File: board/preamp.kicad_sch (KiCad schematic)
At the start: 16 parts, among them SW2 200MDP1T2B2M2, U5 MAX4062

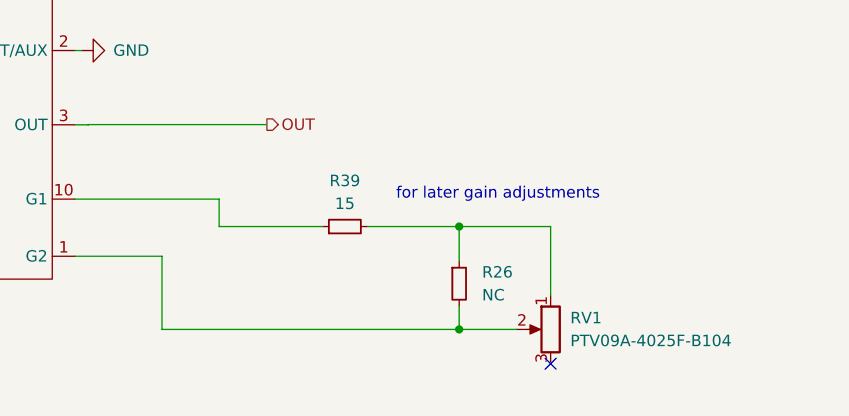
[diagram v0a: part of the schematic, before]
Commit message: option for poti inversion and some missing connections
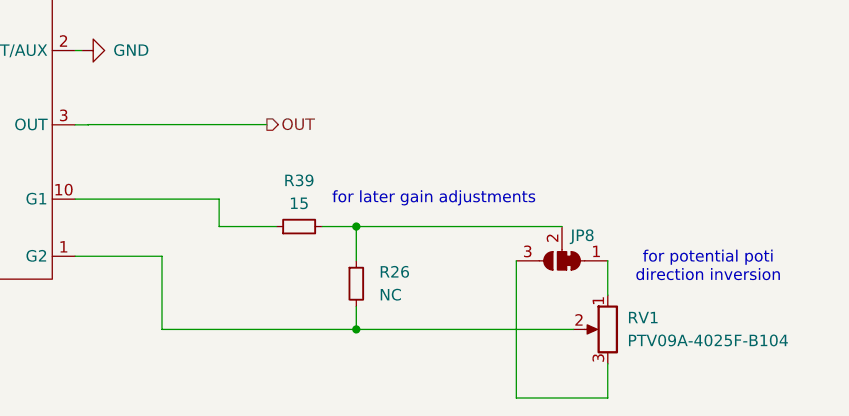
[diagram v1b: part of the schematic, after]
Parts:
- added JP8: SolderJumper_3_Bridged12, Jumper:SolderJumper-3_P1.3mm_Bridged12_RoundedPad1.0x1.5mm, symbol Jumper:SolderJumper_3_Bridged12
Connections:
- net at R26.1, R39.2: now also JP8.2 (C); no longer RV1.1
- net at RV1.3: now also JP8.3 (B)
- new net: JP8.1 (A), RV1.1
- no-connect marks 1 -> 0
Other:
- note added: "for potential poti direction inversion"
- moved on the sheet: R26, R39, RV1
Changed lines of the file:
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@@
 	(paper "A4")
+	(junction
+		(at 228.6 99.06)
+		(diameter 0)
+		(color 0 0 0 0)
+	)
 	(junction
 		(at 154.94 62.23)
@@
 	)
 	(junction
-		(at 240.03 87.63)
-		(diameter 0)
-		(color 0 0 0 0)
-	)
-	(junction
 		(at 78.486 79.629)
 		(diameter 0)
@@
 	)
 	(junction
-		(at 240.03 99.06)
-		(diameter 0)
-		(color 0 0 0 0)
-	)
-	(junction
 		(at 180.34 46.99)
 		(diameter 0)
@@
 	)
 	(junction
+		(at 228.6 87.63)
+		(diameter 0)
+		(color 0 0 0 0)
+	)
+	(junction
 		(at 92.583 83.693)
 		(diameter 0)
 		(color 0 0 0 0)
 	)
-	(no_connect
-		(at 250.19 102.87)
-	)
 	(wire
 		(pts
@@
 	(wire
 		(pts
+			(xy 256.54 102.87) (xy 256.54 106.68)
+		)
+		(stroke
+			(width 0)
+			(type default)
+		)
+	)
+	(wire
+		(pts
 			(xy 180.34 44.45) (xy 180.34 46.99)
 		)
@@
 	(wire
 		(pts
-			(xy 250.19 95.25) (xy 250.19 87.63)
+			(xy 256.54 91.44) (xy 256.54 95.25)
 		)
 		(stroke
@@
 	(wire
 		(pts
-			(xy 240.03 99.06) (xy 240.03 96.52)
+			(xy 246.38 106.68) (xy 256.54 106.68)
+		)
+		(stroke
+			(width 0)
+			(type default)
+		)
+	)
+	(wire
+		(pts
+			(xy 228.6 99.06) (xy 228.6 96.52)
 		)
 		(stroke
@@
 	(wire
 		(pts
-			(xy 240.03 87.63) (xy 240.03 91.44)
+			(xy 228.6 87.63) (xy 228.6 91.44)
 		)
 		(stroke
@@
 	(wire
 		(pts
-			(xy 229.87 87.63) (xy 240.03 87.63)
+			(xy 224.79 87.63) (xy 228.6 87.63)
 		)
 		(stroke
@@
 	(wire
 		(pts
+			(xy 246.38 91.44) (xy 246.38 106.68)
+		)
+		(stroke
+			(width 0)
+			(type default)
+		)
+	)
+	(wire
+		(pts
 			(xy 185.42 49.53) (xy 185.42 46.99)
 		)
@@
 	(wire
 		(pts
-			(xy 240.03 87.63) (xy 250.19 87.63)
-		)
-		(stroke
-			(width 0)
-			(type default)
-		)
-	)
-	(wire
-		(pts
 			(xy 144.78 62.23) (xy 148.59 62.23)
 		)
@@
 	(wire
 		(pts
-			(xy 207.01 99.06) (xy 240.03 99.06)
+			(xy 207.01 99.06) (xy 228.6 99.06)
 		)
 		(stroke
@@
 	(wire
 		(pts
+			(xy 228.6 87.63) (xy 251.46 87.63)
+		)
+		(stroke
+			(width 0)
+			(type default)
+		)
+	)
+	(wire
+		(pts
 			(xy 74.422 87.249) (xy 74.422 92.71)
 		)
@@
 	(wire
 		(pts
-			(xy 240.03 99.06) (xy 246.38 99.06)
-		)
-		(stroke
-			(width 0)
-			(type default)
-		)
-	)
-	(wire
-		(pts
 			(xy 185.42 55.88) (xy 185.42 54.61)
 		)
@@
 	(wire
 		(pts
-			(xy 213.36 87.63) (xy 224.79 87.63)
+			(xy 213.36 87.63) (xy 219.71 87.63)
 		)
 		(stroke
@@
 		(pts
 			(xy 157.6578 89.027) (xy 164.973 89.027)
+		)
+		(stroke
+			(width 0)
+			(type default)
+		)
+	)
+	(wire
+		(pts
+			(xy 228.6 99.06) (xy 252.73 99.06)
 		)
 		(stroke
@@
 	(text "for later gain adjustments"
 		(exclude_from_sim no)
-		(at 244.348 84.074 0)
+		(at 237.236 84.582 0)
+		(effects
+			(font
+				(size 1.27 1.27)
+			)
+		)
+	)
+	(text "for potential poti\ndirection inversion"
+		(exclude_from_sim no)
+		(at 267.716 92.202 0)
 		(effects
 			(font
@@
 	(symbol
 		(lib_id "Device:R_Small")
-		(at 240.03 93.98 0)
+		(at 228.6 93.98 0)
 		(unit 1)
 		(exclude_from_sim no)
@@
 		(fields_autoplaced yes)
 		(property "Reference" "R26"
-			(at 242.57 92.7099 0)
+			(at 231.14 92.7099 0)
 			(effects
 				(font
@@
 		)
 		(property "Value" "NC"
-			(at 242.57 95.2499 0)
+			(at 231.14 95.2499 0)
 			(effects
 				(font
@@
 		)
 		(property "Footprint" "Resistor_THT:R_Axial_DIN0207_L6.3mm_D2.5mm_P10.16mm_Horizontal"
-			(at 240.03 93.98 0)
+			(at 228.6 93.98 0)
 			(effects
 				(font
@@
 		)
 		(property "Datasheet" "~"
-			(at 240.03 93.98 0)
+			(at 228.6 93.98 0)
 			(effects
 				(font
@@
 		)
 		(property "Description" "Resistor, small symbol"
-			(at 240.03 93.98 0)
+			(at 228.6 93.98 0)
 			(effects
 				(font
@@
 		)
 		(property "Sim.Device" ""
-			(at 240.03 93.98 0)
+			(at 228.6 93.98 0)
 			(effects
 				(font
@@
 		)
 		(property "Sim.Pins" ""
-			(at 240.03 93.98 0)
+			(at 228.6 93.98 0)
 			(effects
 				(font
@@
 		)
 		(property "Sim.Type" ""
-			(at 240.03 93.98 0)
+			(at 228.6 93.98 0)
 			(effects
 				(font
@@
 	)
 	(symbol
+		(lib_id "Jumper:SolderJumper_3_Bridged12")
+		(at 251.46 91.44 180)
+		(unit 1)
+		(exclude_from_sim yes)
+		(in_bom no)
+		(on_board yes)
+		(dnp no)
+		(property "Reference" "JP8"
+			(at 253.746 88.646 0)
+			(effects
+				(font
+					(size 1.27 1.27)
+				)
+			)
+		)
+		(property "Value" "SolderJumper_3_Bridged12"
+			(at 251.46 97.79 0)
+			(effects
+				(font
+					(size 1.27 1.27)
+				)
+				(hide yes)
+			)
+		)
+		(property "Footprint" "Jumper:SolderJumper-3_P1.3mm_Bridged12_RoundedPad1.0x1.5mm"
+			(at 251.46 91.44 0)
+			(effects
+				(font
+					(size 1.27 1.27)
+				)
+				(hide yes)
+			)
+		)
+		(property "Datasheet" "~"
+			(at 251.46 91.44 0)
+			(effects
+				(font
+					(size 1.27 1.27)
+				)
+				(hide yes)
+			)
+		)
+		(property "Description" "3-pole Solder Jumper, pins 1+2 closed/bridged"
+			(at 251.46 91.44 0)
+			(effects
+				(font
+					(size 1.27 1.27)
+				)
+				(hide yes)
+			)
+		)
+		(pin "2"
+		)
+		(pin "3"
+		)
+		(pin "1"
+		)
+		(instances
+			(project "spider2"
+				(path "/31073f88-a990-4ecc-8ab9-bb6b56c98e1e/ef17f1e3-6d4b-48c3-ada3-a0af083f4146"
+					(reference "JP8")
+					(unit 1)
+				)
+				(path "/31073f88-a990-4ecc-8ab9-bb6b56c98e1e/5a710a45-03d0-4177-b57a-0573a00e8cb4"
+					(reference "JP9")
+					(unit 1)
+				)
+			)
+		)
+	)
+	(symbol
 		(lib_id "power:+3.3VA")
 		(at 180.34 44.45 0)
@@
 	(symbol
 		(lib_id "Device:R_Potentiometer")
-		(at 250.19 99.06 0)
+		(at 256.54 99.06 0)
 		(mirror y)
 		(unit 1)
@@
 		(dnp no)
 		(property "Reference" "RV1"
-			(at 252.3744 97.79 0)
+			(at 258.7244 97.79 0)
 			(effects
 				(font
@@
 		)
 		(property "Value" "PTV09A-4025F-B104"
-			(at 252.3744 100.33 0)
+			(at 258.7244 100.33 0)
 			(effects
 				(font
@@
 		)
 		(property "Footprint" "Potentiometer_THT:Potentiometer_Bourns_PTV09A-1_Single_Vertical"
-			(at 250.19 99.06 0)
+			(at 256.54 99.06 0)
 			(effects
 				(font
@@
 		)
 		(property "Datasheet" "~"
-			(at 250.19 99.06 0)
+			(at 256.54 99.06 0)
 			(effects
 				(font
@@
 		)
 		(property "Description" "Potentiometer"
-			(at 250.19 99.06 0)
+			(at 256.54 99.06 0)
 			(effects
 				(font
@@
 		)
 		(property "Sim.Device" ""
-			(at 250.19 99.06 0)
+			(at 256.54 99.06 0)
 			(effects
 				(font
@@
 		)
 		(property "Sim.Pins" ""
-			(at 250.19 99.06 0)
+			(at 256.54 99.06 0)
 			(effects
 				(font
@@
 		)
 		(property "Sim.Type" ""
-			(at 250.19 99.06 0)
+			(at 256.54 99.06 0)
 			(effects
 				(font
@@
 	(symbol
 		(lib_id "Device:R_Small")
-		(at 227.33 87.63 90)
+		(at 222.25 87.63 90)
 		(unit 1)
 		(exclude_from_sim no)
@@
 		(fields_autoplaced yes)
 		(property "Reference" "R39"
-			(at 227.33 82.55 90)
+			(at 222.25 82.55 90)
 			(effects
 				(font
@@
 		)
 		(property "Value" "15"
-			(at 227.33 85.09 90)
+			(at 222.25 85.09 90)
 			(effects
 				(font
@@
 		)
 		(property "Footprint" "Resistor_THT:R_Axial_DIN0207_L6.3mm_D2.5mm_P10.16mm_Horizontal"
-			(at 227.33 87.63 0)
+			(at 222.25 87.63 0)
 			(effects
 				(font
@@
 		)
 		(property "Datasheet" "~"
-			(at 227.33 87.63 0)
+			(at 222.25 87.63 0)
 			(effects
 				(font
@@
 		)
 		(property "Description" "Resistor, small symbol"
-			(at 227.33 87.63 0)
+			(at 222.25 87.63 0)
 			(effects
 				(font
@@
 		)
 		(property "Sim.Device" ""
-			(at 227.33 87.63 0)
+			(at 222.25 87.63 0)
 			(effects
 				(font
@@
 		)
 		(property "Sim.Pins" ""
-			(at 227.33 87.63 0)
+			(at 222.25 87.63 0)
 			(effects
 				(font
@@
 		)
 		(property "Sim.Type" ""
-			(at 227.33 87.63 0)
-			(effects
-				(font
+			(at 222.25 87.63 0)
+			(effects
+				(font

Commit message: some cleanups
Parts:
- C31, R26, R42: now not fitted; now left out of the parts list
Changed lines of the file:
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@@
 		(unit 1)
 		(exclude_from_sim no)
-		(in_bom yes)
-		(on_board yes)
-		(dnp no)
+		(in_bom no)
+		(on_board yes)
+		(dnp yes)
 		(fields_autoplaced yes)
 		(property "Reference" "R26"
@@
 			)
 		)
-		(property "Datasheet" "~"
+		(property "Datasheet" "https://eu.mouser.com/datasheet/2/140/200-3304369.pdf"
 			(at 112.522 78.613 0)
 			(effects
@@
 			)
 		)
-		(property "Datasheet" "~"
+		(property "Datasheet" "https://www.bourns.com/docs/product-datasheets/PTV09.pdf"
 			(at 256.54 99.06 0)
 			(effects
@@
 		(unit 1)
 		(exclude_from_sim no)
-		(in_bom yes)
-		(on_board yes)
-		(dnp no)
+		(in_bom no)
+		(on_board yes)
+		(dnp yes)
 		(fields_autoplaced yes)
 		(property "Reference" "R42"
@@
 			)
 		)
-		(property "Datasheet" "~"
+		(property "Datasheet" "https://eu.mouser.com/datasheet/2/140/200-3304369.pdf"
 			(at 112.649 90.17 0)
 			(effects
@@
 		(unit 1)
 		(exclude_from_sim no)
-		(in_bom yes)
-		(on_board yes)
-		(dnp no)
+		(in_bom no)
+		(on_board yes)
+		(dnp yes)
 		(fields_autoplaced yes)
 		(property "Reference" "C31"

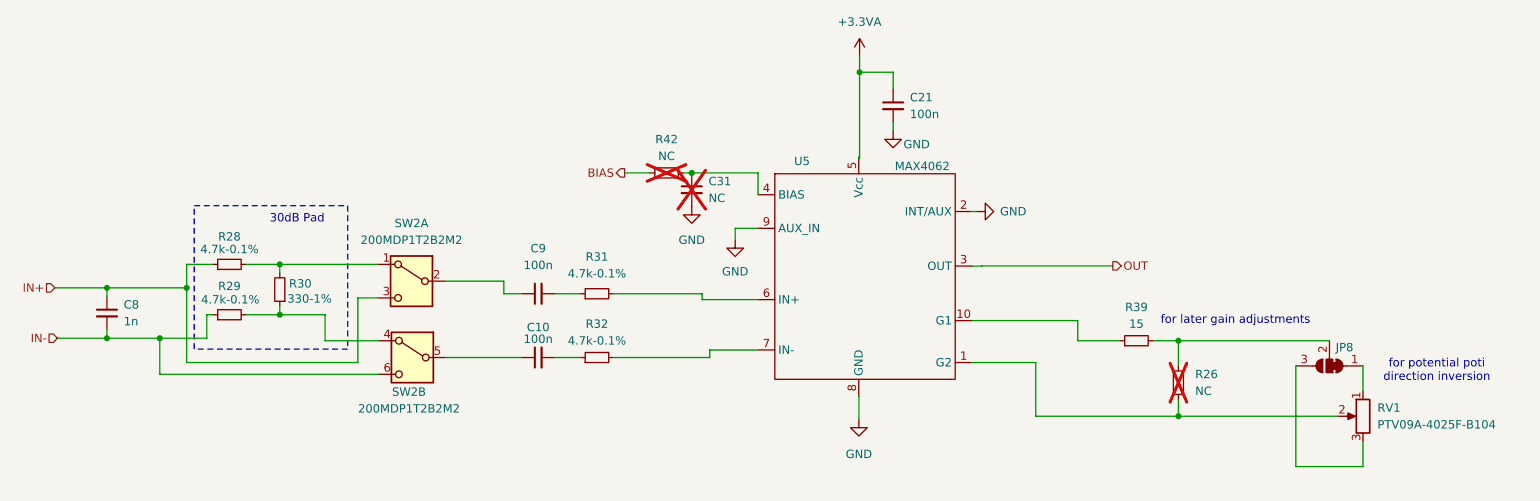
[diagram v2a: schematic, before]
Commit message: throw out not required pad (-30dB for line signals)
the gain range via poti is sufficient enough for line and mics
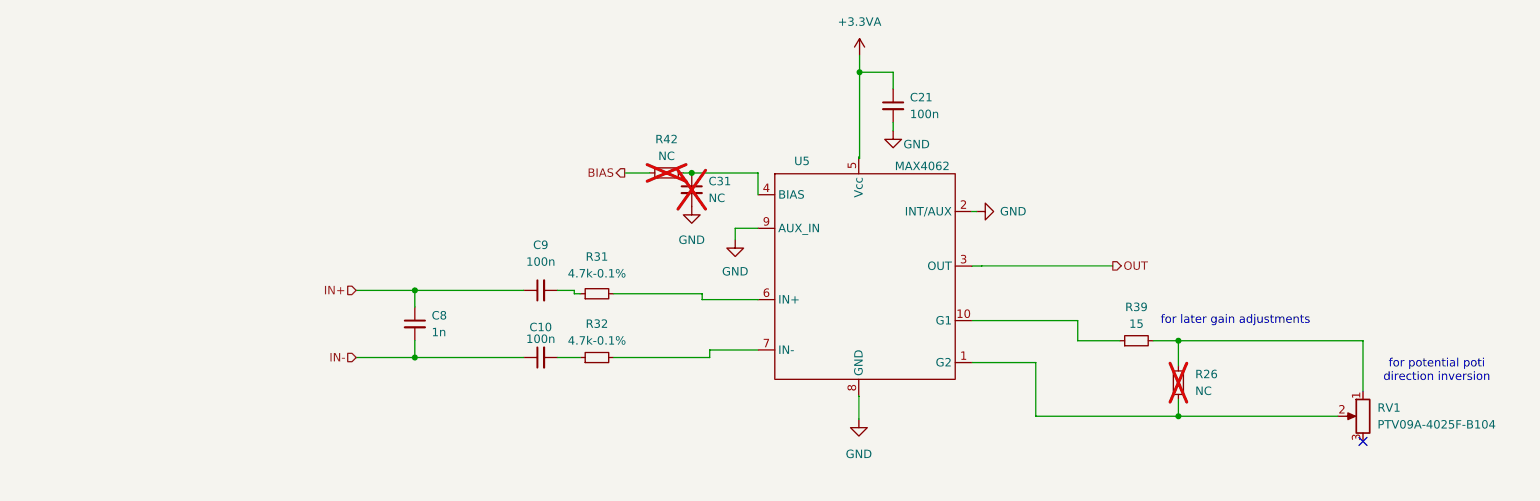
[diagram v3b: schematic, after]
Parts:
- removed JP8: SolderJumper_3_Bridged12, Jumper:SolderJumper-3_P1.3mm_Bridged12_RoundedPad1.0x1.5mm, symbol Jumper:SolderJumper_3_Bridged12
- removed R28, R29: 4.7k-0.1%, Resistor_THT:R_Axial_DIN0207_L6.3mm_D2.5mm_P10.16mm_Horizontal, symbol Device:R_Small
- removed R30: 330-1%, Resistor_THT:R_Axial_DIN0207_L6.3mm_D2.5mm_P10.16mm_Horizontal, symbol Device:R_Small
- removed SW2: 200MDP1T2B2M2, custom:SW_PUSH_E-Switch_200MDPxTxBxM2, symbol Switch:SW_DPDT_x2
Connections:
- net IN+: now also C9.1
- net IN-: now also C10.1
- net at R26.1, R39.2: now also RV1.1
- no-connect marks 0 -> 1
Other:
- note removed: "30dB Pad"
- moved on the sheet: C8, C9

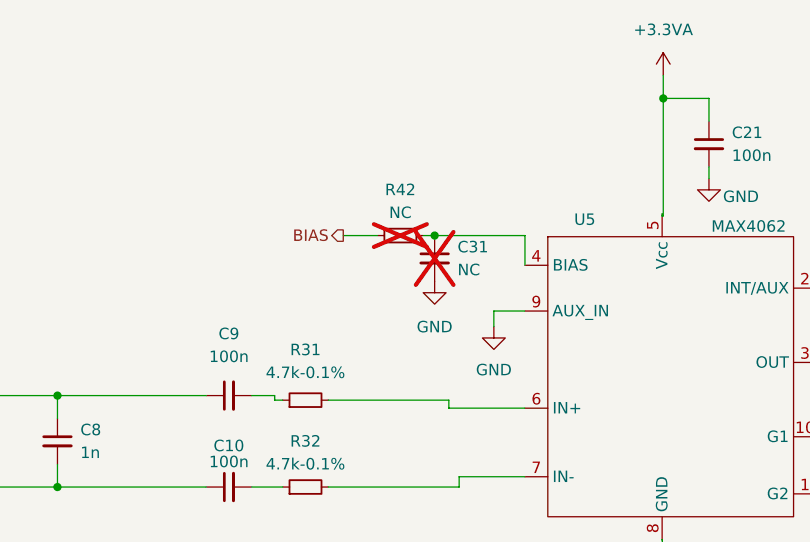
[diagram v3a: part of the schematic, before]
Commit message: clean up not required components
jumpers, some dnp components, etc.
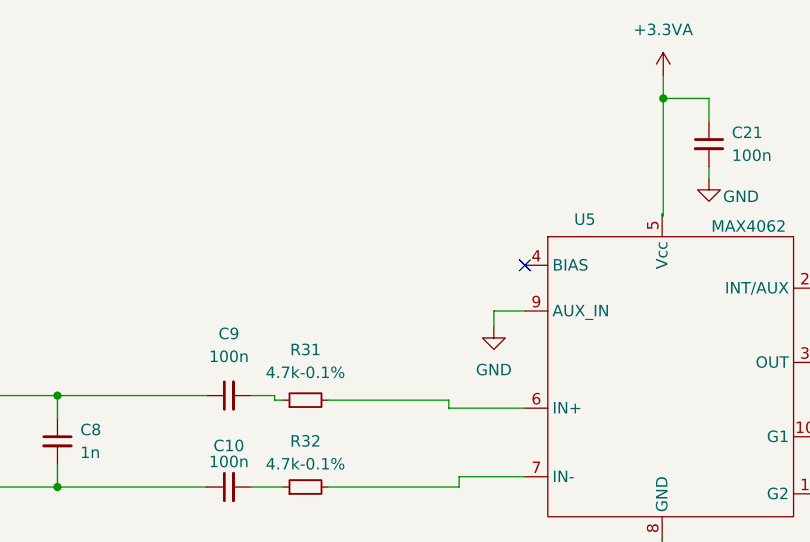
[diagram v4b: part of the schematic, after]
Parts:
- removed C31: NC, Capacitor_SMD:C_0805_2012Metric_Pad1.18x1.45mm_HandSolder, symbol Device:C_Small
- removed R42: NC, Resistor_SMD:R_0805_2012Metric_Pad1.20x1.40mm_HandSolder, symbol Device:R_Small
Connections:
- no-connect marks 1 -> 2

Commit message: bypass capacitor footprints smaller and closer
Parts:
- C21: footprint Capacitor_THT:C_Disc_D5.1mm_W3.2mm_P5.00mm -> Capacitor_THT:C_Disc_D4.3mm_W1.9mm_P5.00mm
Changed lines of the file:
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@@
 			)
 		)
-		(property "Footprint" "Capacitor_THT:C_Disc_D5.1mm_W3.2mm_P5.00mm"
+		(property "Footprint" "Capacitor_THT:C_Disc_D4.3mm_W1.9mm_P5.00mm"
 			(at 185.42 52.07 0)
 			(effects

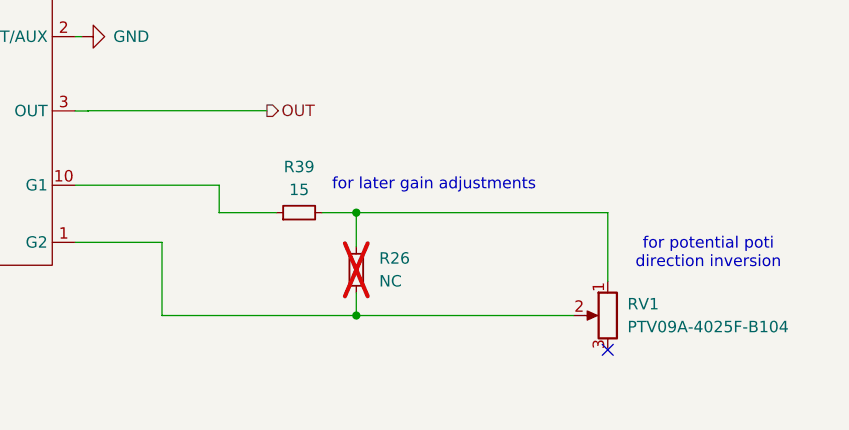
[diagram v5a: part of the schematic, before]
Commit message: multiple changes
- correct transistor footprints
- swap led green/red
- PAM input resistor
- poti adjustments
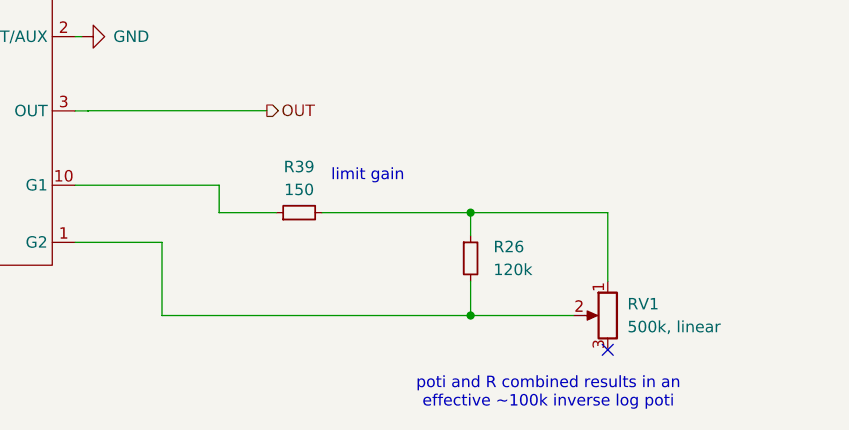
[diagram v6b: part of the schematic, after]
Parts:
- R26: value NC -> 120k; now fitted
- R39: value 15 -> 150
- RV1: value PTV09A-4025F-B104 -> 500k, linear
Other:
- note added: "limit gain"
- note added: "poti and R combined results in an effective ~100k inverse log poti"
- note removed: "for later gain adjustments"
- note removed: "for potential poti direction inversion"
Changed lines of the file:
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@@
 	(paper "A4")
-	(junction
-		(at 228.6 99.06)
-		(diameter 0)
-		(color 0 0 0 0)
-	)
 	(junction
 		(at 113.03 80.01)
@@
 	)
 	(junction
+		(at 241.3 99.06)
+		(diameter 0)
+		(color 0 0 0 0)
+	)
+	(junction
+		(at 241.3 87.63)
+		(diameter 0)
+		(color 0 0 0 0)
+	)
+	(junction
 		(at 113.03 90.17)
 		(diameter 0)
 		(color 0 0 0 0)
 	)
-	(junction
-		(at 228.6 87.63)
-		(diameter 0)
-		(color 0 0 0 0)
-	)
 	(no_connect
 		(at 256.54 102.87)
@@
 	(wire
 		(pts
-			(xy 228.6 99.06) (xy 228.6 96.52)
+			(xy 241.3 99.06) (xy 241.3 95.25)
+		)
+		(stroke
+			(width 0)
+			(type default)
+		)
+	)
+	(wire
+		(pts
+			(xy 241.3 87.63) (xy 256.54 87.63)
 		)
 		(stroke
@@
 	(wire
 		(pts
-			(xy 228.6 87.63) (xy 228.6 91.44)
+			(xy 241.3 87.63) (xy 241.3 90.17)
 		)
 		(stroke
@@
 	(wire
 		(pts
-			(xy 224.79 87.63) (xy 228.6 87.63)
-		)
-		(stroke
-			(width 0)
-			(type default)
-		)
-	)
-	(wire
-		(pts
-			(xy 228.6 87.63) (xy 256.54 87.63)
+			(xy 224.79 87.63) (xy 241.3 87.63)
 		)
 		(stroke
@@
 	(wire
 		(pts
+			(xy 241.3 99.06) (xy 252.73 99.06)
+		)
+		(stroke
+			(width 0)
+			(type default)
+		)
+	)
+	(wire
+		(pts
 			(xy 134.62 80.01) (xy 137.16 80.01)
 		)
@@
 	(wire
 		(pts
-			(xy 207.01 99.06) (xy 228.6 99.06)
+			(xy 207.01 99.06) (xy 241.3 99.06)
 		)
 		(stroke
@@
 		)
 	)
-	(wire
-		(pts
-			(xy 228.6 99.06) (xy 252.73 99.06)
-		)
-		(stroke
-			(width 0)
-			(type default)
-		)
-	)
-	(text "for later gain adjustments"
+	(text "limit gain"
 		(exclude_from_sim no)
-		(at 237.236 84.582 0)
+		(at 229.87 83.566 0)
 		(effects
 			(font
@@
 		)
 	)
-	(text "for potential poti\ndirection inversion"
+	(text "poti and R combined results in an\neffective ~100k inverse log poti"
 		(exclude_from_sim no)
-		(at 267.716 92.202 0)
+		(at 249.936 107.696 0)
 		(effects
 			(font
@@
 	(symbol
 		(lib_id "Device:R_Small")
-		(at 228.6 93.98 0)
+		(at 241.3 92.71 0)
 		(unit 1)
 		(exclude_from_sim no)
 		(in_bom no)
 		(on_board yes)
-		(dnp yes)
+		(dnp no)
 		(fields_autoplaced yes)
 		(property "Reference" "R26"
-			(at 231.14 92.7099 0)
+			(at 243.84 91.4399 0)
 			(effects
 				(font
@@
 			)
 		)
-		(property "Value" "NC"
-			(at 231.14 95.2499 0)
+		(property "Value" "120k"
+			(at 243.84 93.9799 0)
 			(effects
 				(font
@@
 		)
 		(property "Footprint" "Resistor_THT:R_Axial_DIN0207_L6.3mm_D2.5mm_P10.16mm_Horizontal"
-			(at 228.6 93.98 0)
+			(at 241.3 92.71 0)
 			(effects
 				(font
@@
 		)
 		(property "Datasheet" "~"
-			(at 228.6 93.98 0)
+			(at 241.3 92.71 0)
 			(effects
 				(font
@@
 		)
 		(property "Description" "Resistor, small symbol"
-			(at 228.6 93.98 0)
+			(at 241.3 92.71 0)
 			(effects
 				(font
@@
 		)
 		(property "Sim.Device" ""
-			(at 228.6 93.98 0)
+			(at 241.3 92.71 0)
 			(effects
 				(font
@@
 		)
 		(property "Sim.Pins" ""
-			(at 228.6 93.98 0)
+			(at 241.3 92.71 0)
 			(effects
 				(font
@@
 		)
 		(property "Sim.Type" ""
-			(at 228.6 93.98 0)
+			(at 241.3 92.71 0)
 			(effects
 				(font
@@
 			)
 		)
-		(property "Value" "PTV09A-4025F-B104"
+		(property "Value" "500k, linear"
 			(at 258.7244 100.33 0)
 			(effects
@@
 			)
 		)
-		(property "Value" "15"
+		(property "Value" "150"
 			(at 222.25 85.09 90)
 			(effects
